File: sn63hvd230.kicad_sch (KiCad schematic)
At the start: 9 parts, among them U4 SN65HVD230

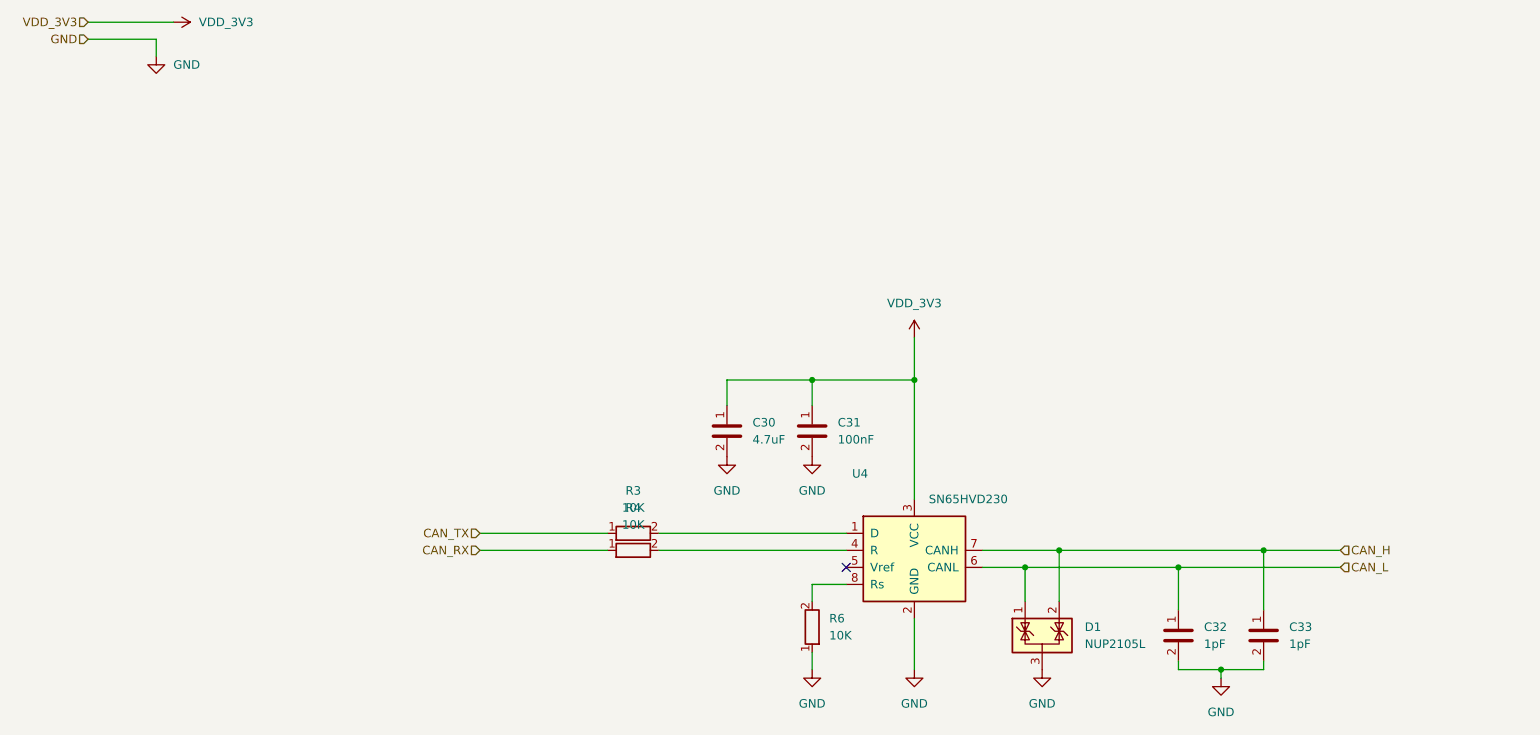
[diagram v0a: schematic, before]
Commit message: feat: added MVP routing implementation
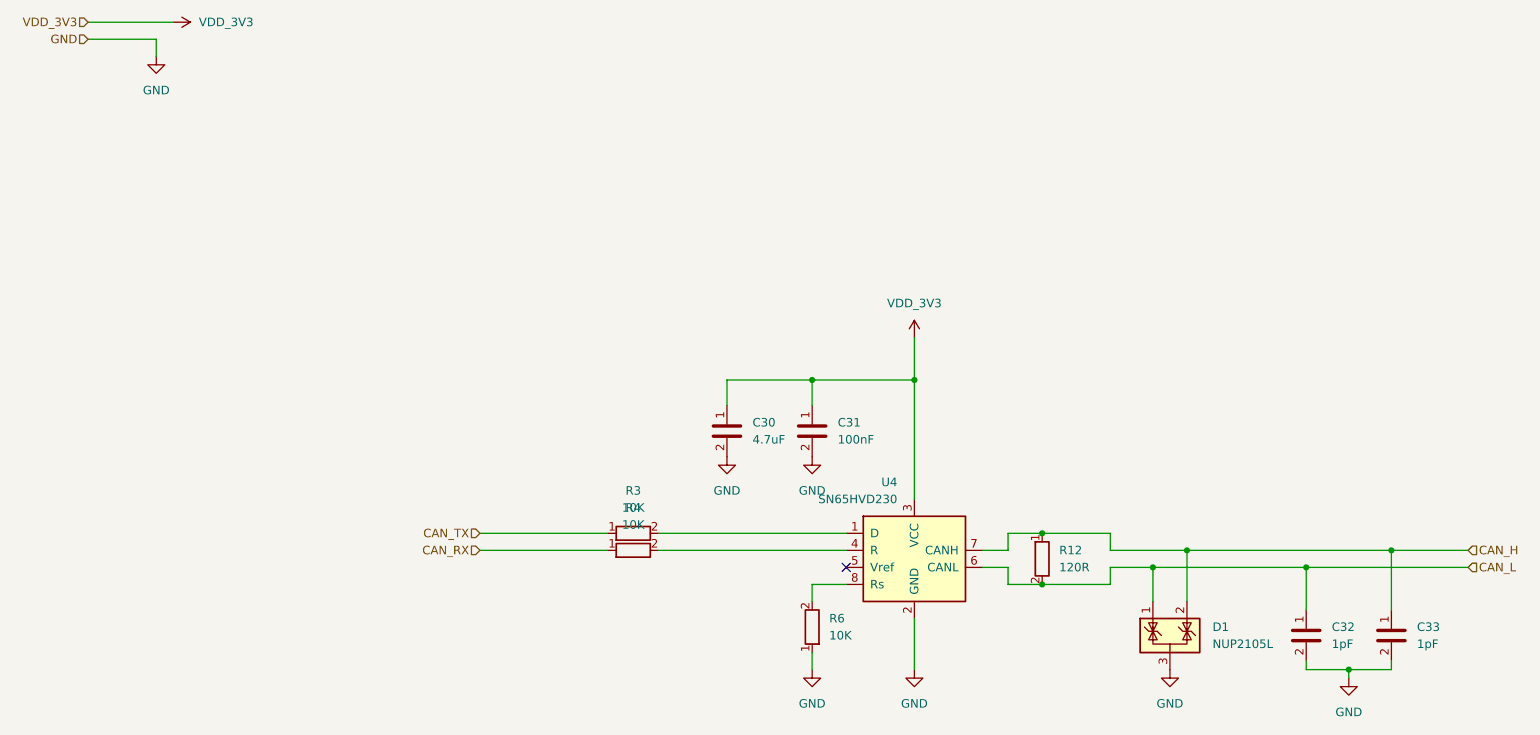
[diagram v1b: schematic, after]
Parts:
- added R12: 120R, chenry-footprint-lib:R_0402, symbol 0_chenry_lib:R_0402_120R
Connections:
- net CAN_H: now also R12.1
- net CAN_L: now also R12.2
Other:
- moved on the sheet: C32, C33, D1

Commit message: fix: final polishes for MFR
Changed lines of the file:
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@@
 		(dnp no)
 		(property "Reference" "D1"
-			(at 193.04 106.6799 0)
+			(at 192.405 105.41 0)
 			(show_name no)
 			(do_not_autoplace no)
@@
 		)
 		(property "Value" "NUP2105L"
-			(at 193.04 109.2199 0)
+			(at 192.405 107.315 0)
 			(show_name no)
 			(do_not_autoplace no)
@@
 		)
 		(property "Value" "GND"
-			(at 148.59 118.11 0)
+			(at 148.59 116.84 0)
 			(show_name no)
 			(do_not_autoplace no)
@@
 		(dnp no)
 		(fields_autoplaced yes)
-		(property "Reference" "#PWR01"
+		(property "Reference" "#PWR1"
 			(at 148.59 67.31 0)
 			(hide yes)
@@
 			(project "Rover VCU"
 				(path "/33c96268-4ca2-4a73-94d6-a3ed4f27d429/49ddb0fd-441a-42bf-83b6-c17defafd145"
-					(reference "#PWR027")
+					(reference "#PWR27")
 					(unit 1)
 				)
 				(path "/33c96268-4ca2-4a73-94d6-a3ed4f27d429/cbe7f1f7-be81-4288-926d-1d0a7b695cd8"
-					(reference "#PWR01")
+					(reference "#PWR1")
 					(unit 1)
 				)
@@
 		(dnp no)
 		(fields_autoplaced yes)
-		(property "Reference" "#PWR048"
+		(property "Reference" "#PWR48"
 			(at 34.29 16.51 0)
 			(hide yes)
@@
 			(project "Rover VCU"
 				(path "/33c96268-4ca2-4a73-94d6-a3ed4f27d429/49ddb0fd-441a-42bf-83b6-c17defafd145"
-					(reference "#PWR055")
+					(reference "#PWR55")
 					(unit 1)
 				)
 				(path "/33c96268-4ca2-4a73-94d6-a3ed4f27d429/cbe7f1f7-be81-4288-926d-1d0a7b695cd8"
-					(reference "#PWR048")
-					(unit 1)
-				)
+					(reference "#PWR48")
+					(unit 1)
+				)
